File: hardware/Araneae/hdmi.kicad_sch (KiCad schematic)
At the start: 2 parts, among them J3 HDMI_A

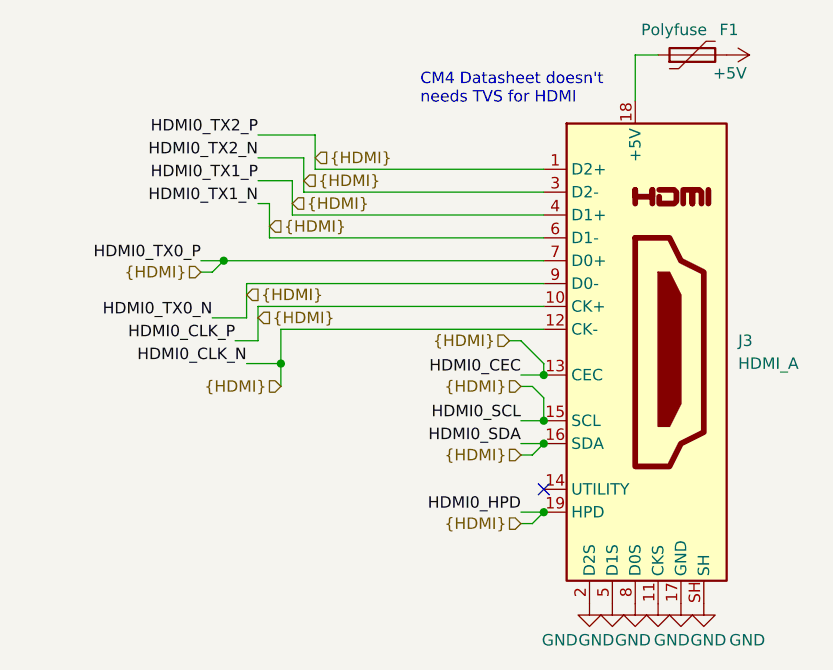
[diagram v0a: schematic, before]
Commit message: Add CI workflow for PCB checks and artifact generation
- Created a GitHub Actions workflow (`ci.yml`) to automate hardware checks including ERC, DRC, and plot generation for KiCad projects.
- Added a new footprint for the SON50P200X200X80-9N component in `SON50P200X200X80-9N.kicad_mod`.
- Introduced a new symbol for the TPS22965DSGR component in `TPS22965DSGR.kicad_sym`.
- Added a configuration file `kibot.yaml` for generating fabrication files and other outputs.
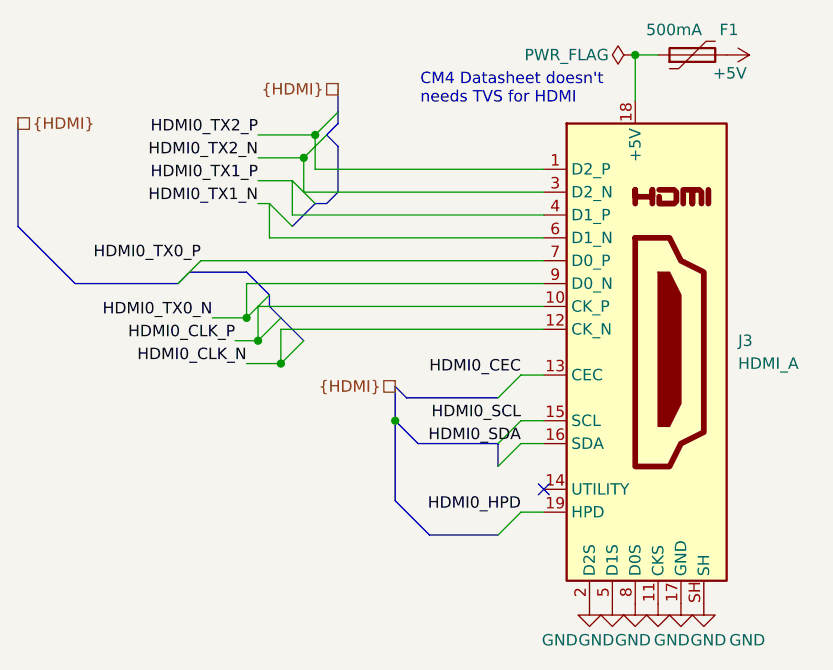
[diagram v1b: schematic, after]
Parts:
- F1: value Polyfuse -> 500mA; footprint (none) -> Fuse:Fuse_1206_3216Metric
- J3: footprint (none) -> Connector_Video:HDMI_A_Molex_208658-1001_Horizontal
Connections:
- net {HDMI}: no longer J3.1 (D2+), J3.10 (CK+), J3.12 (CK-), J3.13 (CEC), J3.15 (SCL), J3.16 (SDA), J3.19 (HPD), J3.3 (D2-), J3.4 (D1+), J3.6 (D1-), J3.7 (D0+), J3.9 (D0-)
- new net HDMI0_CEC: J3.13 (CEC)
- new net HDMI0_CLK_N: J3.12 (CK_N)
- new net HDMI0_CLK_P: J3.10 (CK_P)
- new net HDMI0_HPD: J3.19 (HPD)
- new net HDMI0_SCL: J3.15 (SCL)
- new net HDMI0_SDA: J3.16 (SDA)
- new net HDMI0_TX0_N: J3.9 (D0_N)
- new net HDMI0_TX0_P: J3.7 (D0_P)
- new net HDMI0_TX1_N: J3.6 (D1_N)
- new net HDMI0_TX1_P: J3.4 (D1_P)
- new net HDMI0_TX2_N: J3.3 (D2_N)
- new net HDMI0_TX2_P: J3.1 (D2_P)
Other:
- company: (none) -> Matheus Henrique(Aka: TheusHen)
- title: (none) -> Araneae
